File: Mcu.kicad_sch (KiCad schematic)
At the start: 25 parts, among them U7 STM32H723VGHx, X2 X322516MLB4SI

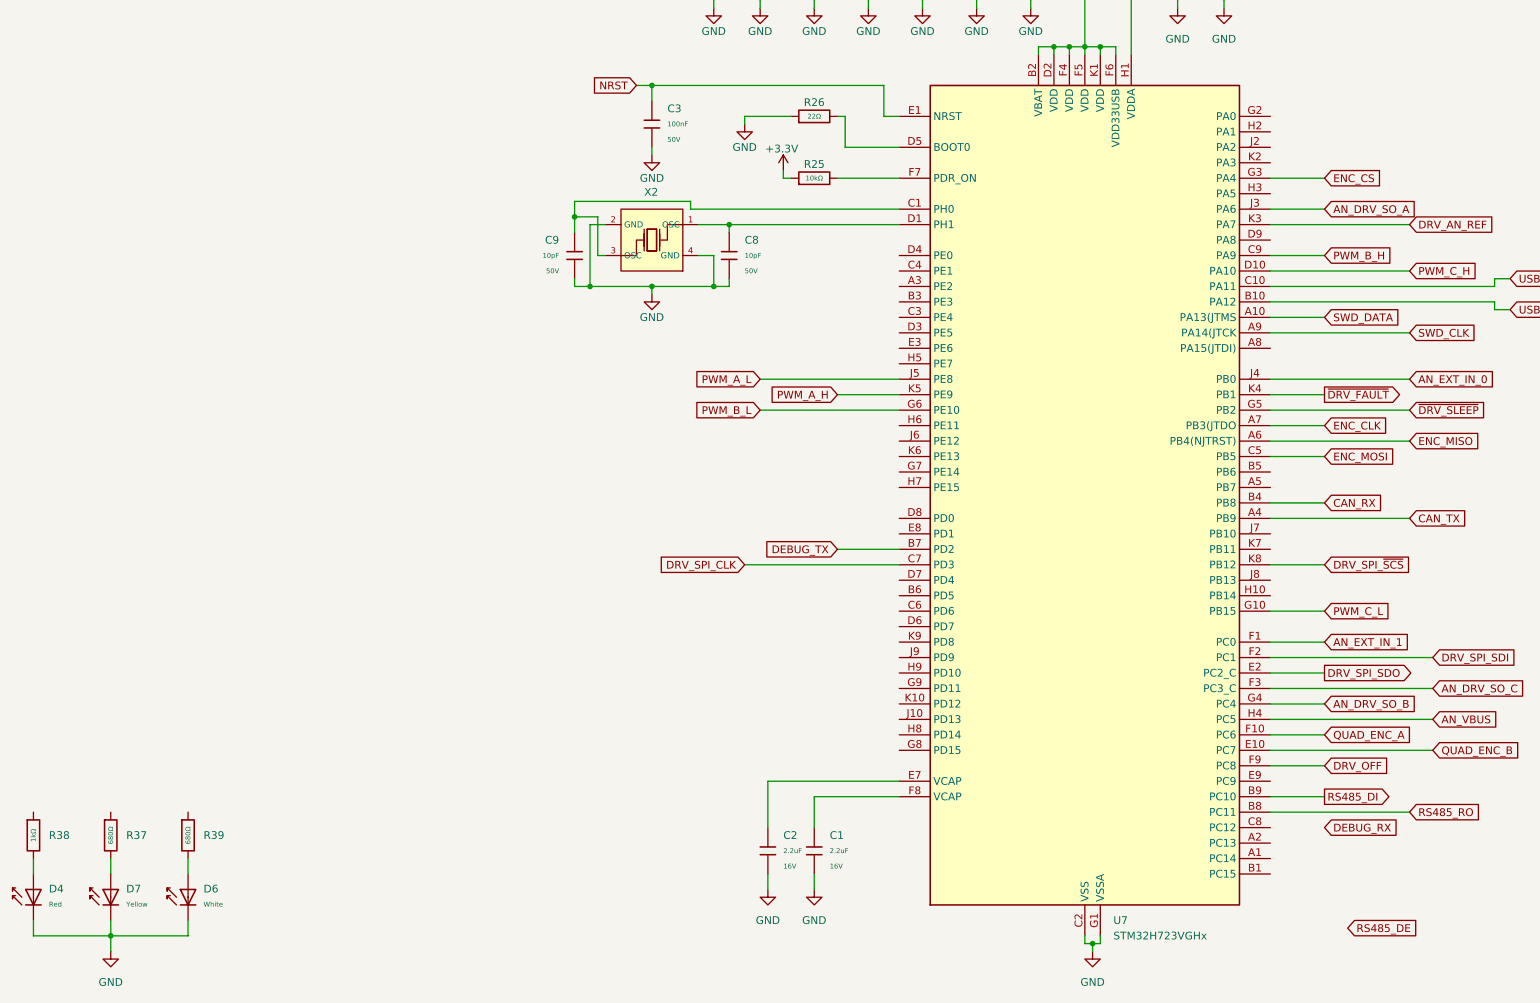
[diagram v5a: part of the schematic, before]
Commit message: Re arrange connectors
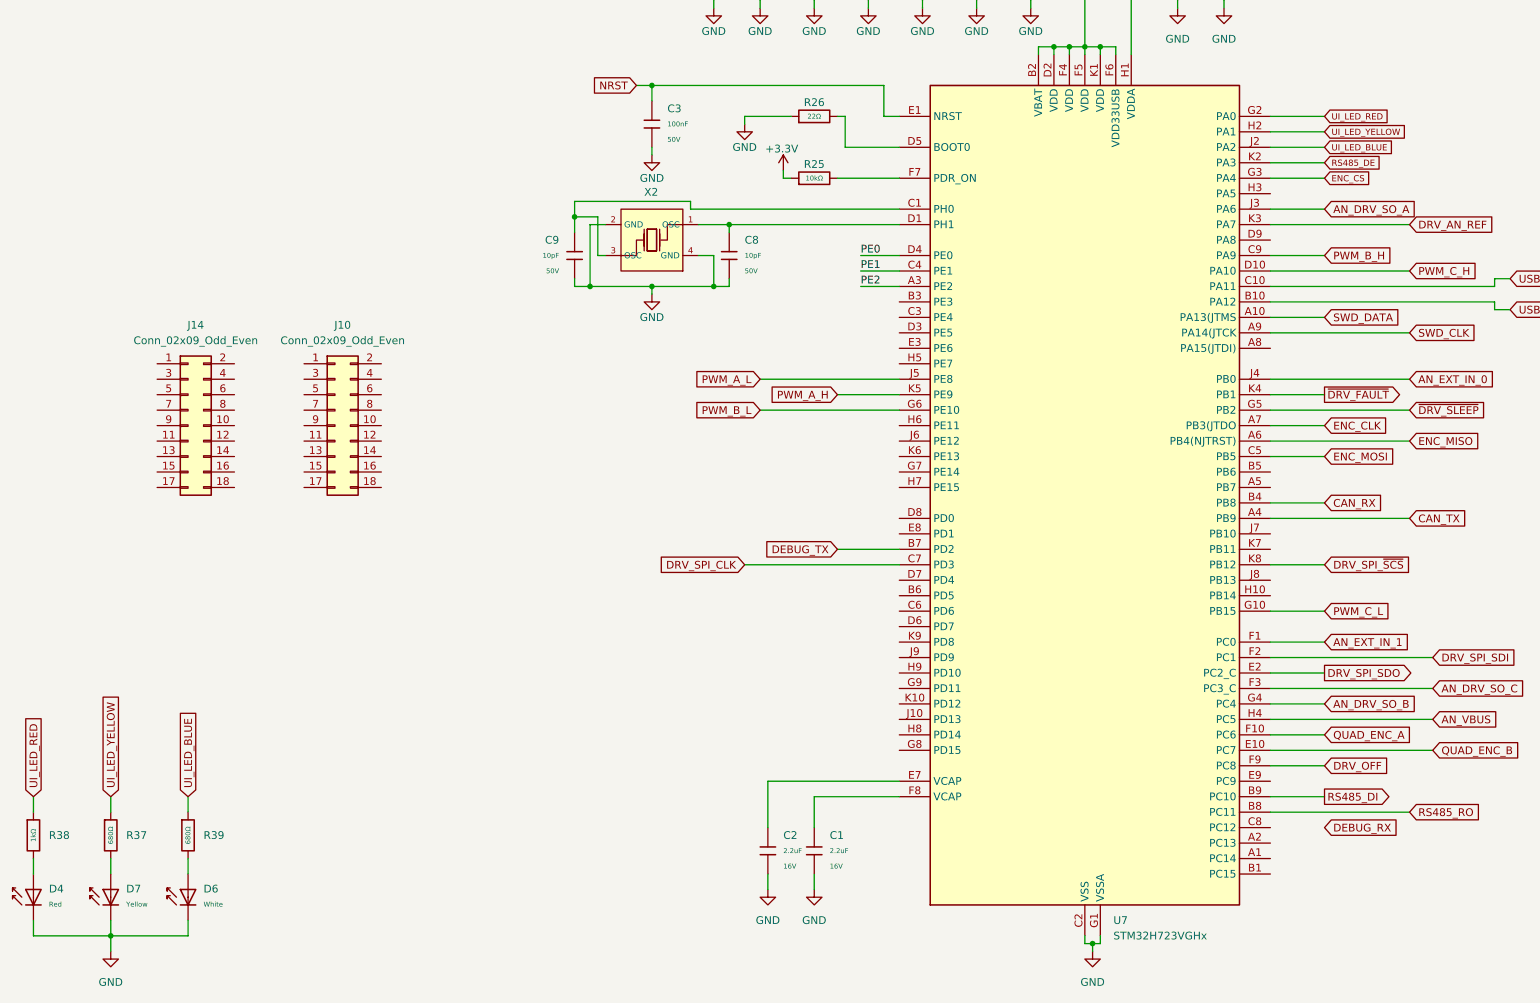
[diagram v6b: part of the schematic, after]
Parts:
- added J10, J14: Conn_02x09_Odd_Even, Connector_PinHeader_2.54mm:PinHeader_2x09_P2.54mm_Vertical, symbol Connector_Generic:Conn_02x09_Odd_Even
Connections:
- net RS485_DE: now also U7.K2 (PA3)
- net UI_LED_RED: now reaches R38.1
- net UI_LED_RED: now also U7.G2 (PA0)
- net UI_LED_YELLOW: now reaches R37.1
- net UI_LED_YELLOW: now also U7.H2 (PA1)
- net UI_LED_BLUE: now reaches R39.1
- net UI_LED_BLUE: now also U7.J2 (PA2)
- net PE2: now reaches U7.A3 (PE2)
- net PE1: now reaches U7.C4 (PE1)
- net PE0: now reaches U7.D4 (PE0)

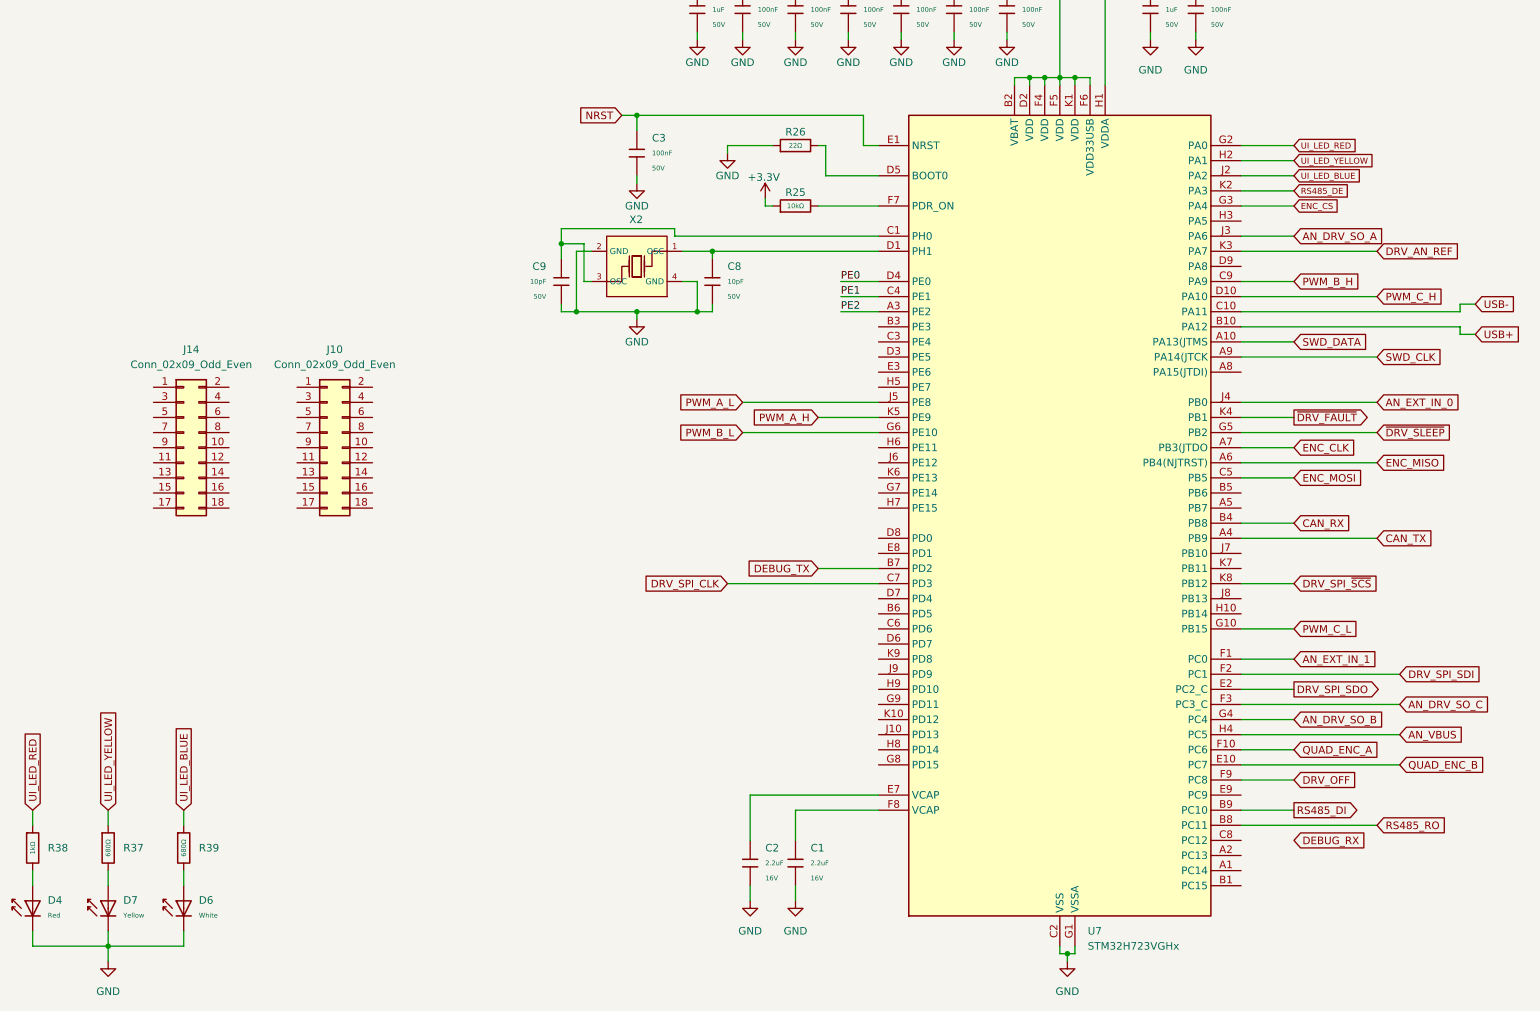
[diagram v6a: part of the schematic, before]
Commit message: updated mcu connections
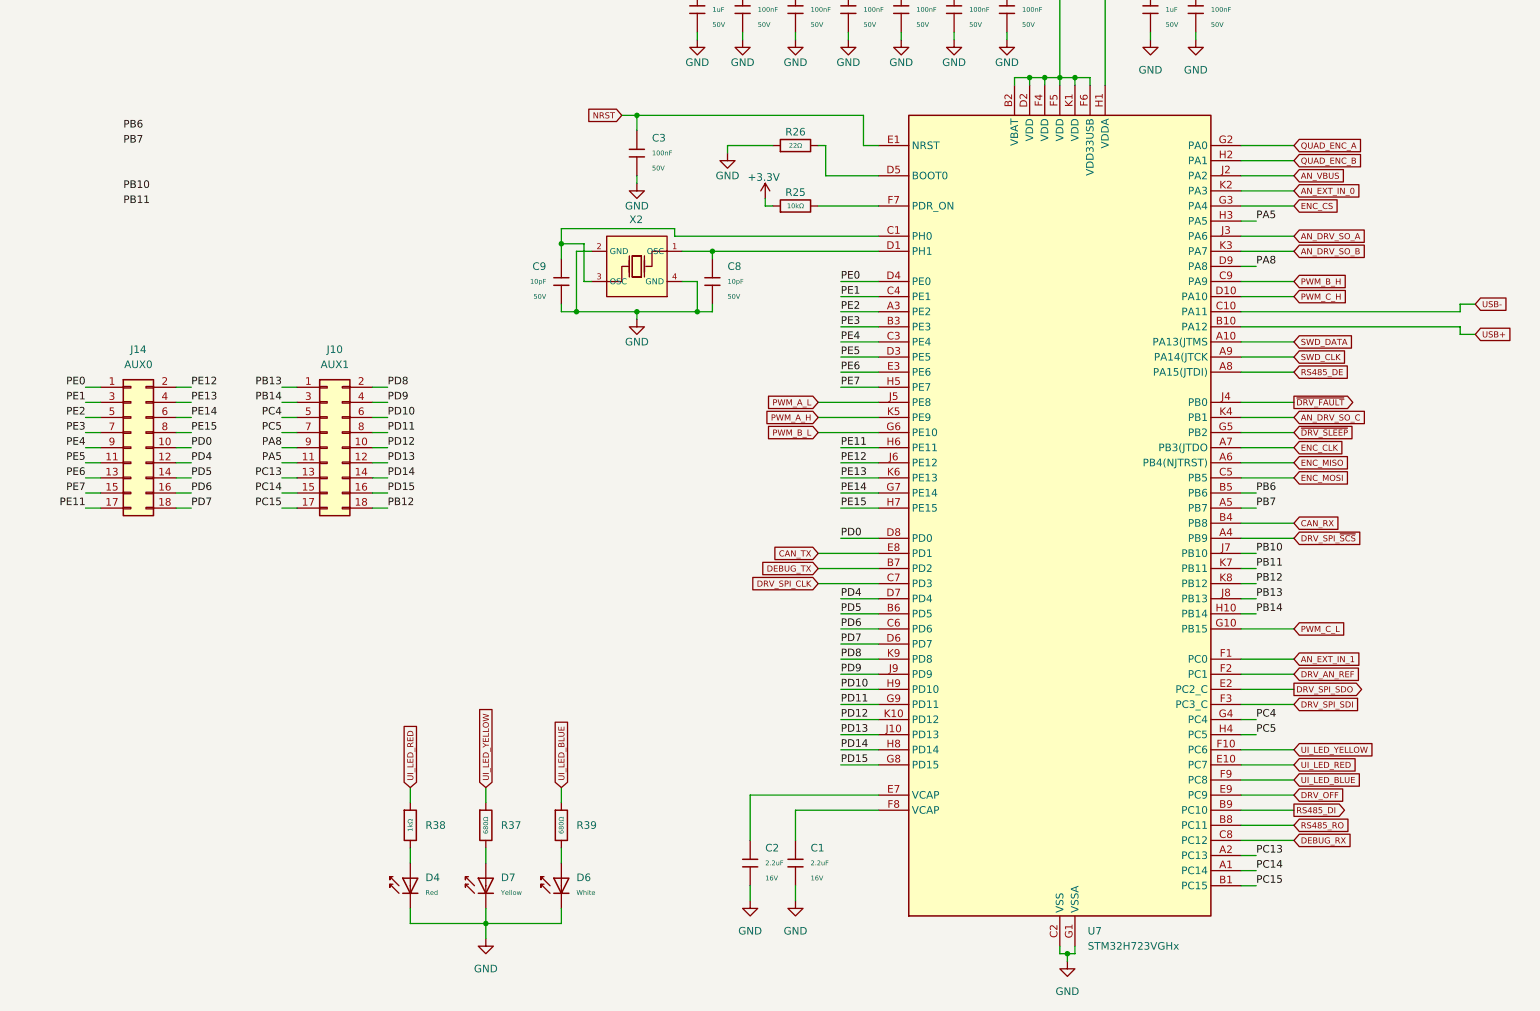
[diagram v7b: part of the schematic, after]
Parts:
- J10: value Conn_02x09_Odd_Even -> AUX1
- J14: value Conn_02x09_Odd_Even -> AUX0
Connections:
- net AN_DRV_SO_B: now also U7.K3 (PA7); no longer U7.G4 (PC4)
- net AN_DRV_SO_C: now also U7.K4 (PB1); no longer U7.F3 (PC3_C)
- net AN_EXT_IN_0: now also U7.K2 (PA3); no longer U7.J4 (PB0)
- net AN_VBUS: now also U7.J2 (PA2); no longer U7.H4 (PC5)
- net CAN_TX: now also U7.E8 (PD1); no longer U7.A4 (PB9)
- net DEBUG_RX: now also U7.C8 (PC12)
- net DRV_AN_REF: now also U7.F2 (PC1); no longer U7.K3 (PA7)
- net DRV_OFF: now also U7.E9 (PC9); no longer U7.F9 (PC8)
- net DRV_SPI_SDI: now also U7.F3 (PC3_C); no longer U7.F2 (PC1)
- net DRV_SPI_~{SCS}: now also U7.A4 (PB9); no longer U7.K8 (PB12)
- net PE0: now also J14.1 (Pin_1)
- net PE1: now also J14.3 (Pin_3)
- net PE2: now also J14.5 (Pin_5)
- net QUAD_ENC_A: now also U7.G2 (PA0); no longer U7.F10 (PC6)
- net QUAD_ENC_B: now also U7.H2 (PA1); no longer U7.E10 (PC7)
- net RS485_DE: now also U7.A8 (PA15(JTDI)); no longer U7.K2 (PA3)
- net UI_LED_BLUE: now also U7.F9 (PC8); no longer U7.J2 (PA2)
- net UI_LED_RED: now also U7.E10 (PC7); no longer U7.G2 (PA0)
- net UI_LED_YELLOW: now also U7.F10 (PC6); no longer U7.H2 (PA1)
- net ~{DRV_FAULT}: now also U7.J4 (PB0); no longer U7.K4 (PB1)
- net PD0: now reaches J14.10 (Pin_10)
- net PD0: now also U7.D8 (PD0)
- net PE5: now reaches J14.11 (Pin_11)
- net PE5: now also U7.D3 (PE5)
- net PD4: now reaches J14.12 (Pin_12)
- net PD4: now also U7.D7 (PD4)
- net PE6: now reaches J14.13 (Pin_13)
- net PE6: now also U7.E3 (PE6)
- net PD5: now reaches J14.14 (Pin_14)
- net PD5: now also U7.B6 (PD5)
- net PE7: now reaches J14.15 (Pin_15)
- net PE7: now also U7.H5 (PE7)
- net PD6: now reaches J14.16 (Pin_16)
- net PD6: now also U7.C6 (PD6)
- net PE11: now reaches J14.17 (Pin_17)
- net PE11: now also U7.H6 (PE11)
- net PD7: now reaches J14.18 (Pin_18)
- net PD7: now also U7.D6 (PD7)
- net PE12: now reaches J14.2 (Pin_2)
- net PE12: now also U7.J6 (PE12)
- net PE13: now reaches J14.4 (Pin_4)
- net PE13: now also U7.K6 (PE13)
- net PE14: now reaches J14.6 (Pin_6)
- net PE14: now also U7.G7 (PE14)
- net PE3: now reaches J14.7 (Pin_7)
- net PE3: now also U7.B3 (PE3)
- net PE15: now reaches J14.8 (Pin_8)
- net PE15: now also U7.H7 (PE15)
- net PE4: now reaches J14.9 (Pin_9)
- net PE4: now also U7.C3 (PE4)
- net PC14: now reaches U7.A1 (PC14)
- net PC14: now also J10.15 (Pin_15)
- net PC13: now reaches U7.A2 (PC13)
- net PC13: now also J10.13 (Pin_13)
- net PB7: now reaches U7.A5 (PB7)
- net PC15: now reaches U7.B1 (PC15)
- net PC15: now also J10.17 (Pin_17)
- net PB6: now reaches U7.B5 (PB6)
- net PA8: now reaches U7.D9 (PA8)
- net PA8: now also J10.9 (Pin_9)
- net PD15: now reaches U7.G8 (PD15)
- net PD15: now also J10.16 (Pin_16)
- net PD11: now reaches U7.G9 (PD11)
- net PD11: now also J10.8 (Pin_8)
- net PB14: now reaches U7.H10 (PB14)
- net PB14: now also J10.3 (Pin_3)
- net PA5: now reaches U7.H3 (PA5)
- net PA5: now also J10.11 (Pin_11)
- net PD14: now reaches U7.H8 (PD14)
- net PD14: now also J10.14 (Pin_14)
- net PD10: now reaches U7.H9 (PD10)
- net PD10: now also J10.6 (Pin_6)
- net PD13: now reaches U7.J10 (PD13)
- net PD13: now also J10.12 (Pin_12)
- net PB10: now reaches U7.J7 (PB10)
- net PB13: now reaches U7.J8 (PB13)
- net PB13: now also J10.1 (Pin_1)
- net PD9: now reaches U7.J9 (PD9)
- net PD9: now also J10.4 (Pin_4)
- net PD12: now reaches U7.K10 (PD12)
- net PD12: now also J10.10 (Pin_10)
- net PB11: now reaches U7.K7 (PB11)
- net PD8: now reaches U7.K9 (PD8)
- net PD8: now also J10.2 (Pin_2)
- net PB12: now reaches J10.18 (Pin_18)
- net PB12: now also U7.K8 (PB12)
- net PC4: now reaches J10.5 (Pin_5)
- net PC4: now also U7.G4 (PC4)
- net PC5: now reaches J10.7 (Pin_7)
- net PC5: now also U7.H4 (PC5)
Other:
- moved on the sheet: D4, D6, D7, J14, R37, R38, R39

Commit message: layout placement
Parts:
- removed J10: AUX1, Connector_PinHeader_2.54mm:PinHeader_2x09_P2.54mm_Vertical, symbol Connector_Generic:Conn_02x09_Odd_Even
- removed J14: AUX0, Connector_PinHeader_2.54mm:PinHeader_2x09_P2.54mm_Vertical, symbol Connector_Generic:Conn_02x09_Odd_Even
- added J8, J9: AUX0, Connector_PinSocket_2.54mm:PinSocket_2x10_P2.54mm_Vertical, symbol Connector_Generic:Conn_02x10_Odd_Even
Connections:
- net PA5: now also J9.11 (Pin_11)
- net PA8: now also J9.9 (Pin_9)
- net PB10: now also J8.19 (Pin_19)
- net PB11: now also J8.20 (Pin_20)
- net PB12: now also J9.18 (Pin_18)
- net PB13: now also J9.1 (Pin_1)
- net PB14: now also J9.3 (Pin_3)
- net PB6: now also J9.19 (Pin_19)
- net PB7: now also J9.20 (Pin_20)
- net PC13: now also J9.13 (Pin_13)
- net PC14: now also J9.15 (Pin_15)
- net PC15: now also J9.17 (Pin_17)
- net PC4: now also J9.5 (Pin_5)
- net PC5: now also J9.7 (Pin_7)
- net PD0: now also J8.10 (Pin_10)
- net PD10: now also J9.6 (Pin_6)
- net PD11: now also J9.8 (Pin_8)
- net PD12: now also J9.10 (Pin_10)
- net PD13: now also J9.12 (Pin_12)
- net PD14: now also J9.14 (Pin_14)
- net PD15: now also J9.16 (Pin_16)
- net PD4: now also J8.12 (Pin_12)
- net PD5: now also J8.14 (Pin_14)
- net PD6: now also J8.16 (Pin_16)
- net PD7: now also J8.18 (Pin_18)
- net PD8: now also J9.2 (Pin_2)
- net PD9: now also J9.4 (Pin_4)
- net PE0: now also J8.1 (Pin_1)
- net PE1: now also J8.3 (Pin_3)
- net PE11: now also J8.17 (Pin_17)
- net PE12: now also J8.2 (Pin_2)
- net PE13: now also J8.4 (Pin_4)
- net PE14: now also J8.6 (Pin_6)
- net PE15: now also J8.8 (Pin_8)
- net PE2: now also J8.5 (Pin_5)
- net PE3: now also J8.7 (Pin_7)
- net PE4: now also J8.9 (Pin_9)
- net PE5: now also J8.11 (Pin_11)
- net PE6: now also J8.13 (Pin_13)
- net PE7: now also J8.15 (Pin_15)
